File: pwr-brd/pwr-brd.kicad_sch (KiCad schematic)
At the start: 30 parts, among them J1 PWRIN, J2 CTRLIN, J3 PWROUT, J4 PWROUT, J5 PWROUT, J6 PWROUT, U1 TPS27SA08CPWPR, U2 TPS27SA08CPWPR

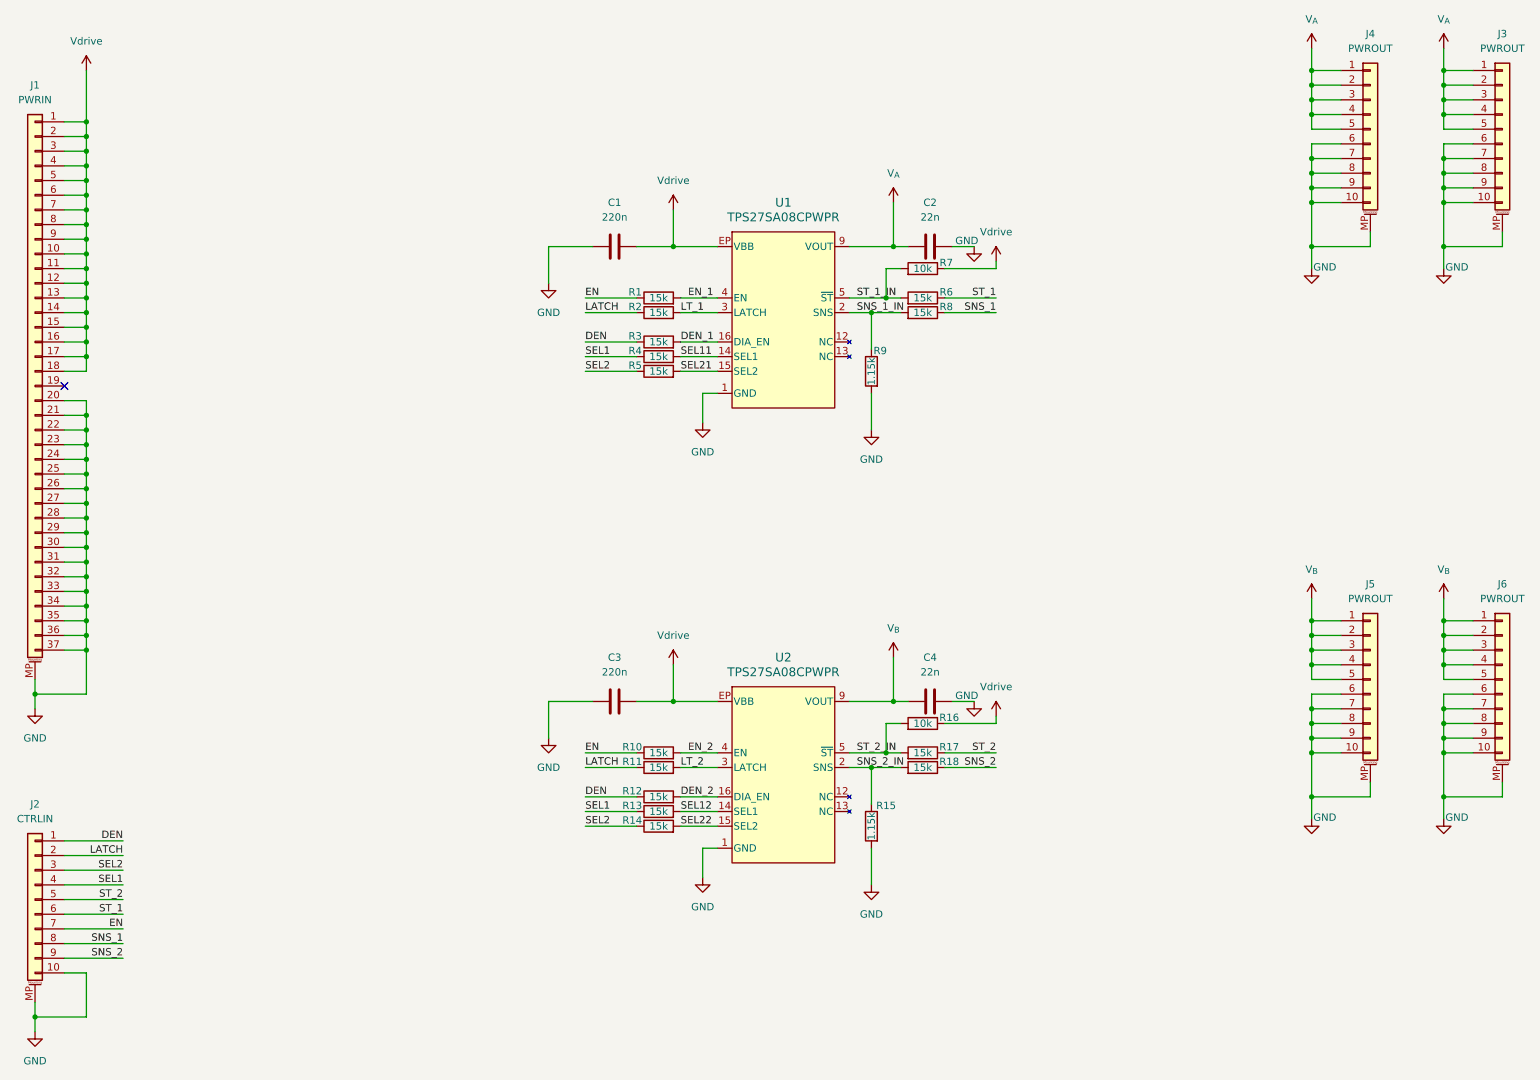
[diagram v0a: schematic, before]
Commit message: Laid out inrush limiter
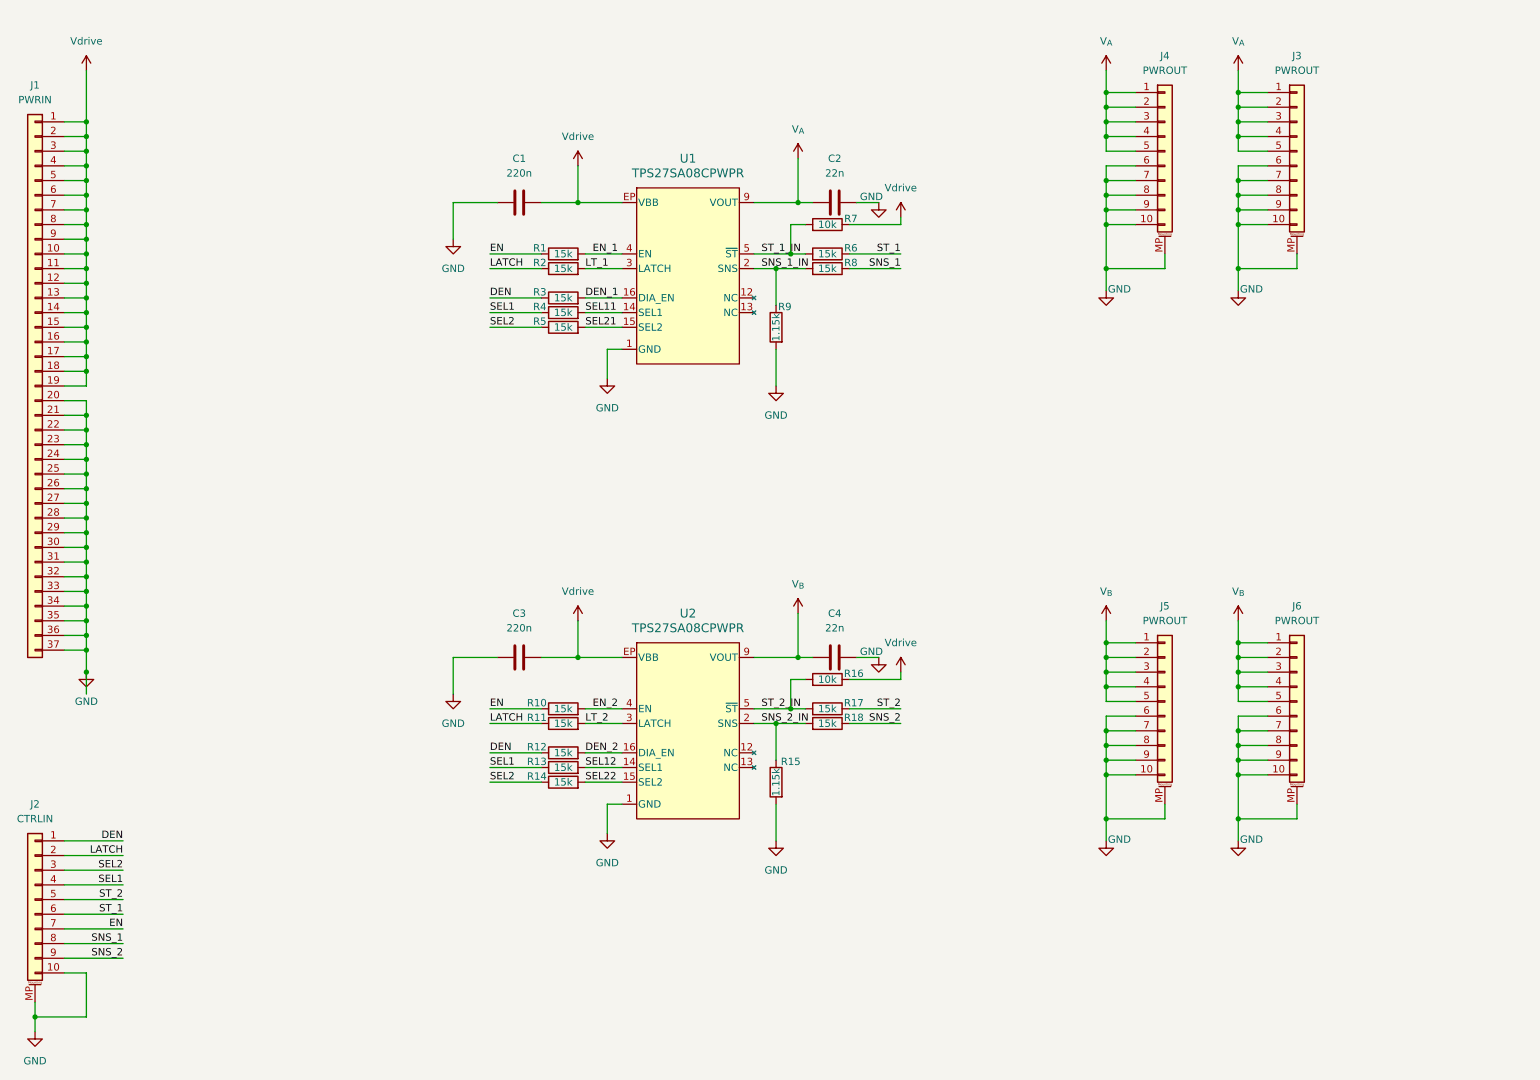
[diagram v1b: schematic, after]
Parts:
- J1: symbol Connector_Generic_MountingPin:Conn_01x37_MountingPin -> Connector_Generic:Conn_01x37
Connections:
- net GND: no longer J1.MP (MountPin)
- net Vdrive: now also J1.19 (Pin_19)
- no-connect marks 1 -> 0
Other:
- company: (none) -> ${COMPANY}
- title: (none) -> ${PRJ_NAME}
- moved on the sheet: C1, C2, C3, C4, J3, J4, J5, J6, R1, R10, R11, R12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
